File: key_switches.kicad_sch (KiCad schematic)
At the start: 3 parts, among them SW1 SW_Push

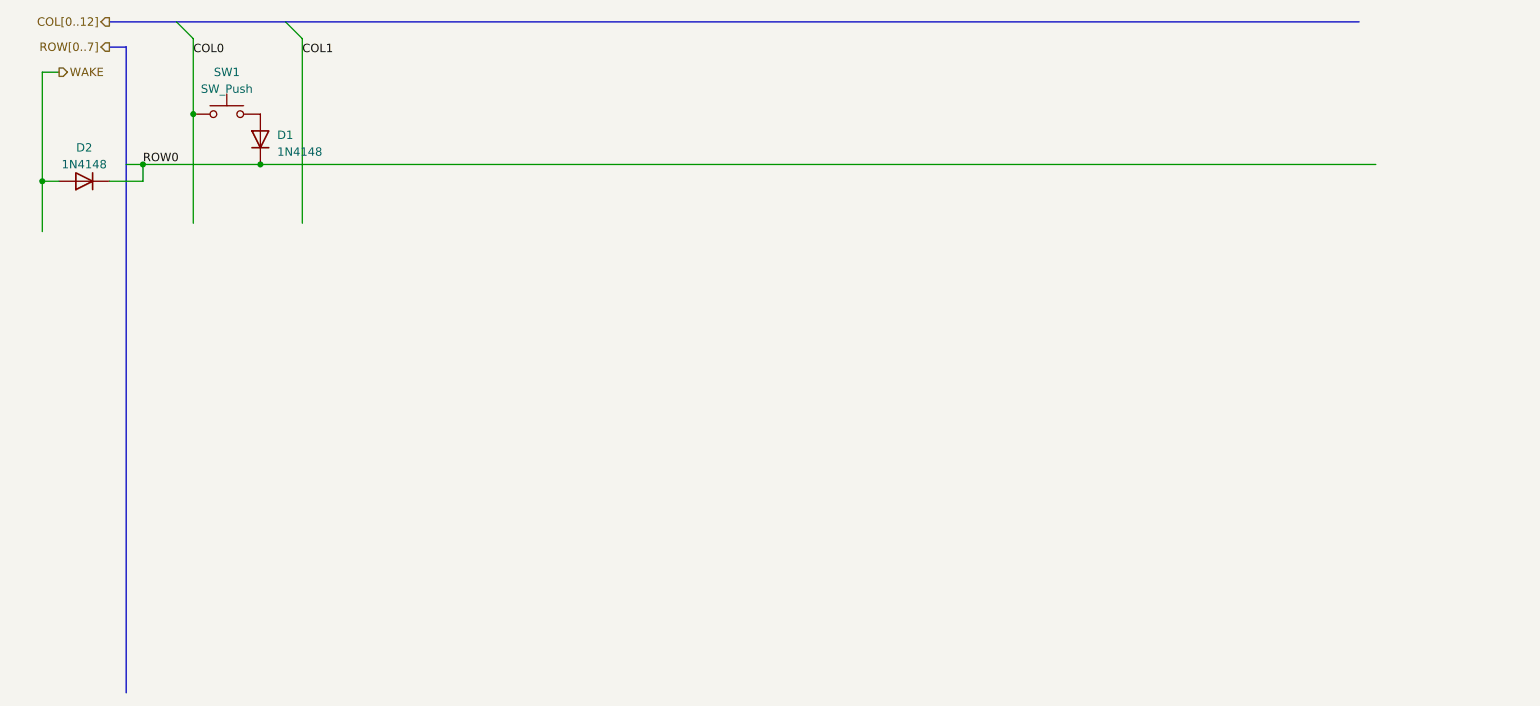
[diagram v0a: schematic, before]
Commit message: added a new key
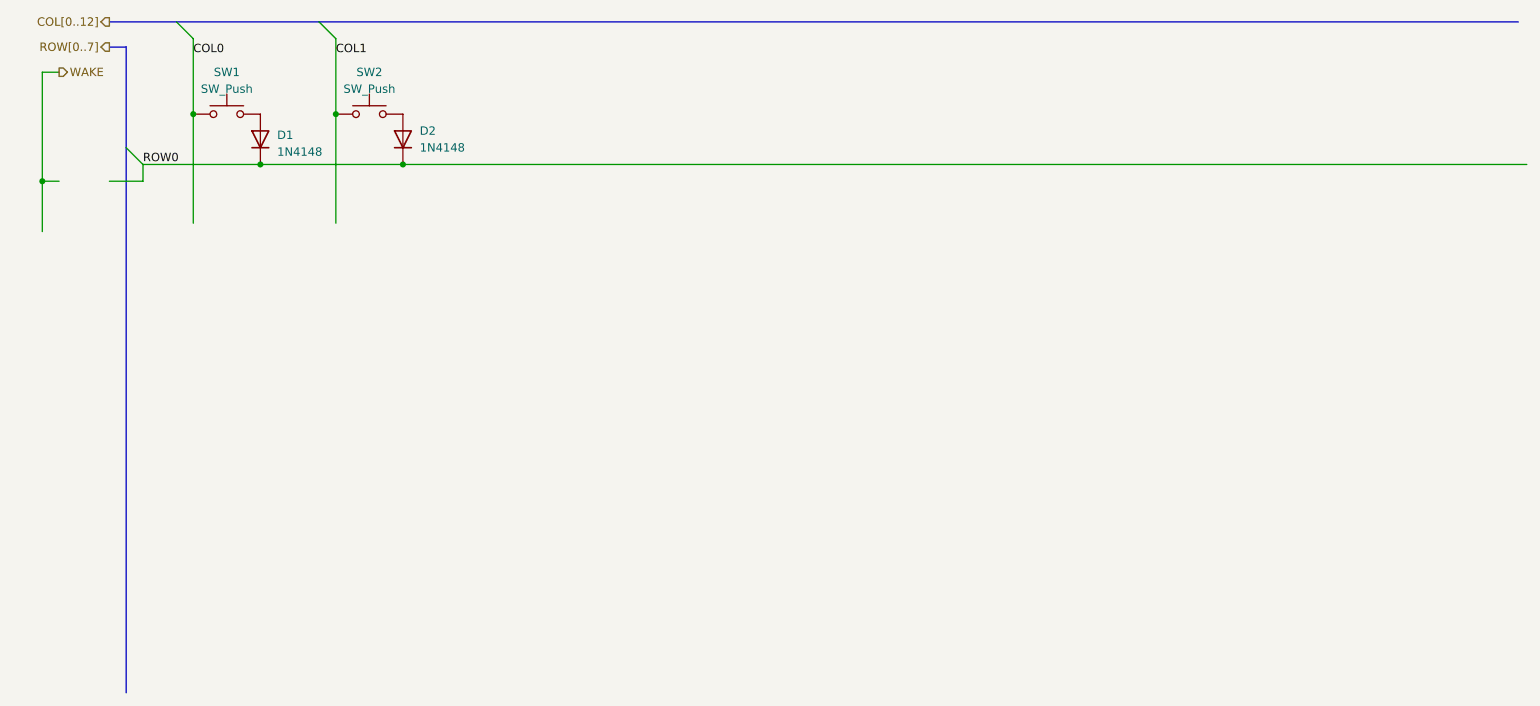
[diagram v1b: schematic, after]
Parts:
- added SW2: SW_Push, symbol Switch:SW_Push
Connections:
- net COL1: now also SW2.1
- net WAKE: no longer D2.2 (A)
- new net: D2.2 (A), SW2.2
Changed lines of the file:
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@@
   (junction (at 19.05 64.77) (diameter 0) (color 0 0 0 0)
   )
+  (junction (at 63.5 54.61) (diameter 0) (color 0 0 0 0)
+  )
   (junction (at 41.91 54.61) (diameter 0) (color 0 0 0 0)
   )
-  (junction (at 34.29 62.23) (diameter 0) (color 0 0 0 0)
+  (junction (at 73.66 62.23) (diameter 0) (color 0 0 0 0)
   )
   (junction (at 52.07 62.23) (diameter 0) (color 0 0 0 0)
@@
     (stroke (width 0) (type default))
   )
-  (bus_entry (at 58.42 43.18) (size -2.54 -2.54)
-    (stroke (width 0) (type default))
-  )
-  (bus (pts (xy 55.88 40.64) (xy 218.44 40.64))
+  (bus_entry (at 63.5 43.18) (size -2.54 -2.54)
+    (stroke (width 0) (type default))
+  )
+  (bus_entry (at 31.75 59.69) (size 2.54 2.54)
+    (stroke (width 0) (type default))
+  )
+  (bus (pts (xy 60.96 40.64) (xy 242.57 40.64))
     (stroke (width 0) (type default))
   )
@@
     (stroke (width 0) (type default))
   )
+  (wire (pts (xy 63.5 43.18) (xy 63.5 54.61))
+    (stroke (width 0) (type default))
+  )
+  (wire (pts (xy 73.66 62.23) (xy 243.84 62.23))
+    (stroke (width 0) (type default))
+  )
+  (wire (pts (xy 19.05 48.26) (xy 19.05 64.77))
+    (stroke (width 0) (type default))
+  )
+  (wire (pts (xy 21.59 48.26) (xy 19.05 48.26))
+    (stroke (width 0) (type default))
+  )
   (wire (pts (xy 34.29 62.23) (xy 52.07 62.23))
     (stroke (width 0) (type default))
   )
-  (wire (pts (xy 58.42 43.18) (xy 58.42 71.12))
-    (stroke (width 0) (type default))
-  )
-  (wire (pts (xy 19.05 48.26) (xy 19.05 64.77))
-    (stroke (width 0) (type default))
-  )
-  (wire (pts (xy 31.75 62.23) (xy 34.29 62.23))
-    (stroke (width 0) (type default))
-  )
-  (wire (pts (xy 21.59 48.26) (xy 19.05 48.26))
-    (stroke (width 0) (type default))
-  )
-  (bus (pts (xy 31.75 44.45) (xy 31.75 142.24))
-    (stroke (width 0) (type default))
-  )
-  (bus (pts (xy 39.37 40.64) (xy 55.88 40.64))
+  (bus (pts (xy 31.75 44.45) (xy 31.75 59.69))
+    (stroke (width 0) (type default))
+  )
+  (bus (pts (xy 39.37 40.64) (xy 60.96 40.64))
     (stroke (width 0) (type default))
   )
@@
     (stroke (width 0) (type default))
   )
-  (wire (pts (xy 52.07 62.23) (xy 220.98 62.23))
+  (wire (pts (xy 52.07 62.23) (xy 73.66 62.23))
+    (stroke (width 0) (type default))
+  )
+  (bus (pts (xy 31.75 59.69) (xy 31.75 142.24))
     (stroke (width 0) (type default))
   )
@@
   )
   (wire (pts (xy 34.29 64.77) (xy 34.29 62.23))
+    (stroke (width 0) (type default))
+  )
+  (wire (pts (xy 63.5 54.61) (xy 63.5 71.12))
     (stroke (width 0) (type default))
   )
@@
     (effects (font (size 1.27 1.27)) (justify left bottom))
   )
-  (label "COL1" (at 58.42 45.72 0) (fields_autoplaced)
+  (label "COL1" (at 63.5 45.72 0) (fields_autoplaced)
     (effects (font (size 1.27 1.27)) (justify left bottom))
   )
@@
     )
   )
-  (symbol (lib_id "Diode:1N4148") (at 25.4 64.77 180) (unit 1)
-    (in_bom yes) (on_board yes) (dnp no) (fields_autoplaced)
-    (property "Reference" "D2" (at 25.4 59.69 0)
-      (effects (font (size 1.27 1.27)))
-    )
-    (property "Value" "1N4148" (at 25.4 62.23 0)
-      (effects (font (size 1.27 1.27)))
-    )
-    (property "Footprint" "Diode_THT:D_DO-35_SOD27_P7.62mm_Horizontal" (at 25.4 64.77 0)
-      (effects (font (size 1.27 1.27)) hide)
-    )
-    (property "Datasheet" "https://assets.nexperia.com/documents/data-sheet/1N4148_1N4448.pdf" (at 25.4 64.77 0)
-      (effects (font (size 1.27 1.27)) hide)
-    )
-    (property "Sim.Device" "D" (at 25.4 64.77 0)
-      (effects (font (size 1.27 1.27)) hide)
-    )
-    (property "Sim.Pins" "1=K 2=A" (at 25.4 64.77 0)
+  (symbol (lib_id "Diode:1N4148") (at 73.66 58.42 90) (unit 1)
+    (in_bom yes) (on_board yes) (dnp no) (fields_autoplaced)
+    (property "Reference" "D2" (at 76.2 57.15 90)
+      (effects (font (size 1.27 1.27)) (justify right))
+    )
+    (property "Value" "1N4148" (at 76.2 59.69 90)
+      (effects (font (size 1.27 1.27)) (justify right))
+    )
+    (property "Footprint" "Diode_THT:D_DO-35_SOD27_P7.62mm_Horizontal" (at 73.66 58.42 0)
+      (effects (font (size 1.27 1.27)) hide)
+    )
+    (property "Datasheet" "https://assets.nexperia.com/documents/data-sheet/1N4148_1N4448.pdf" (at 73.66 58.42 0)
+      (effects (font (size 1.27 1.27)) hide)
+    )
+    (property "Sim.Device" "D" (at 73.66 58.42 0)
+      (effects (font (size 1.27 1.27)) hide)
+    )
+    (property "Sim.Pins" "1=K 2=A" (at 73.66 58.42 0)
       (effects (font (size 1.27 1.27)) hide)
     )
@@
         )
       )
+    )
+  )
+  (symbol (lib_id "Switch:SW_Push") (at 68.58 54.61 0) (unit 1)
+    (in_bom yes) (on_board yes) (dnp no) (fields_autoplaced)
+    (property "Reference" "SW2" (at 68.58 48.26 0)
+      (effects (font (size 1.27 1.27)))
+    )
+    (property "Value" "SW_Push" (at 68.58 50.8 0)
+      (effects (font (size 1.27 1.27)))
+    )
+    (property "Footprint" "" (at 68.58 49.53 0)
+      (effects (font (size 1.27 1.27)) hide)
+    )
+    (property "Datasheet" "~" (at 68.58 49.53 0)
+      (effects (font (size 1.27 1.27)) hide)
+    )
+    (pin "1")
+    (pin "2")
+    (instances
+      (project "Das Keymatrix"
+        (path "/acc36760-ecf2-4bfb-a74b-64a2ca3ad899/b926c080-6ca9-40c9-8789-c9c9b79d063c"
+          (reference "SW2") (unit 1)
+        )
+      )

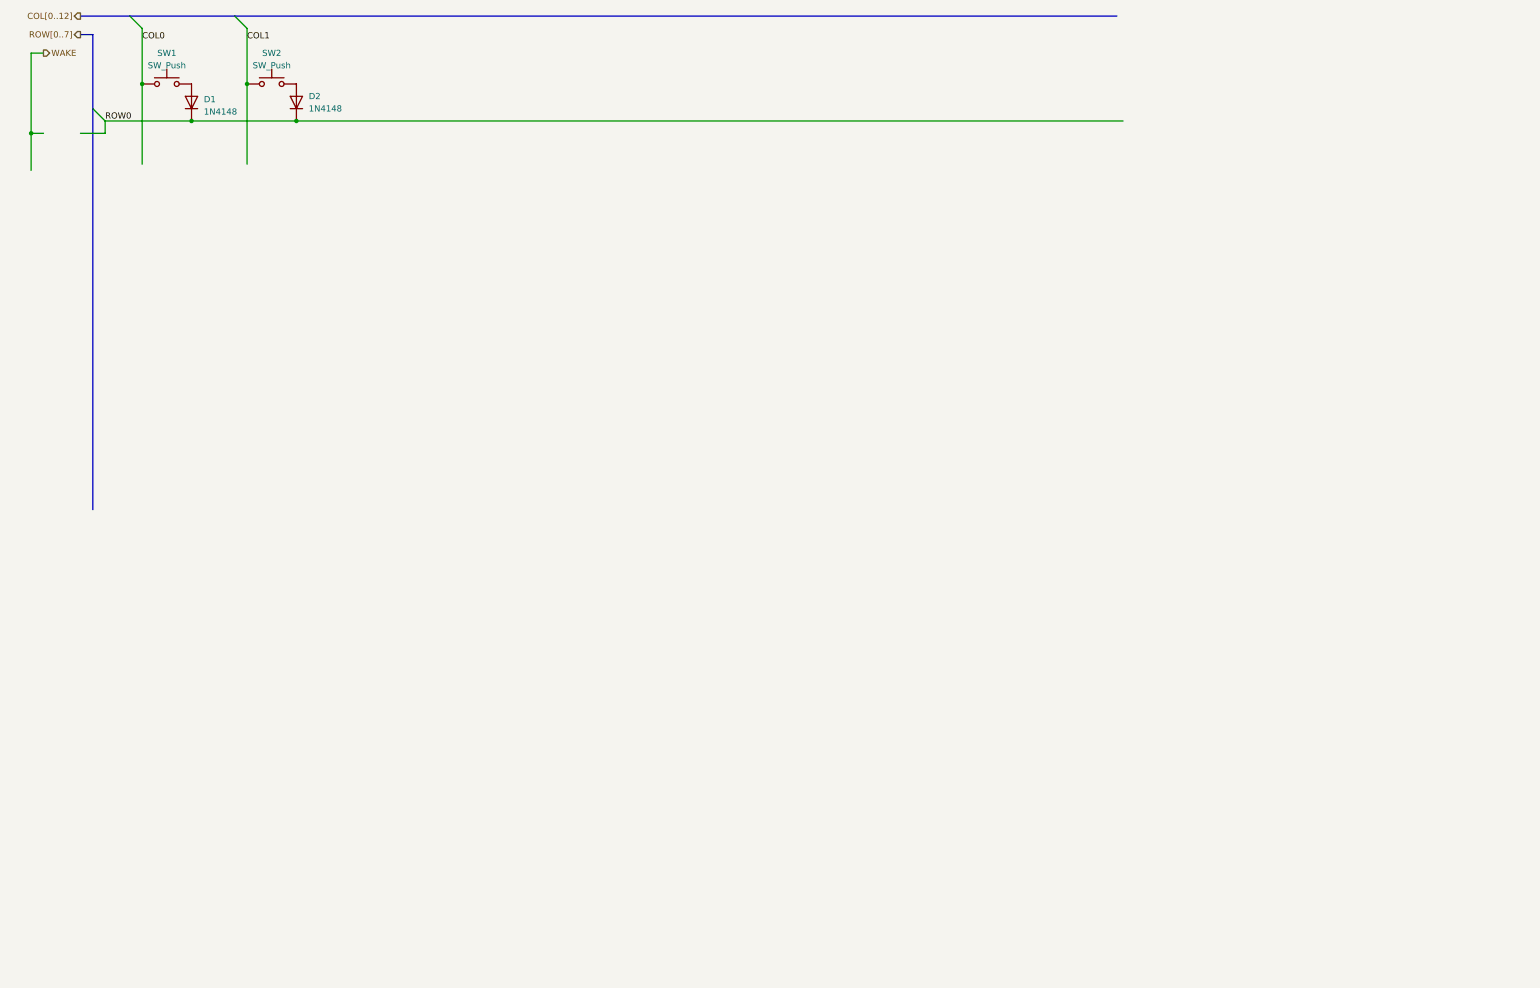
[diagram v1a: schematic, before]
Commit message: added extra switches
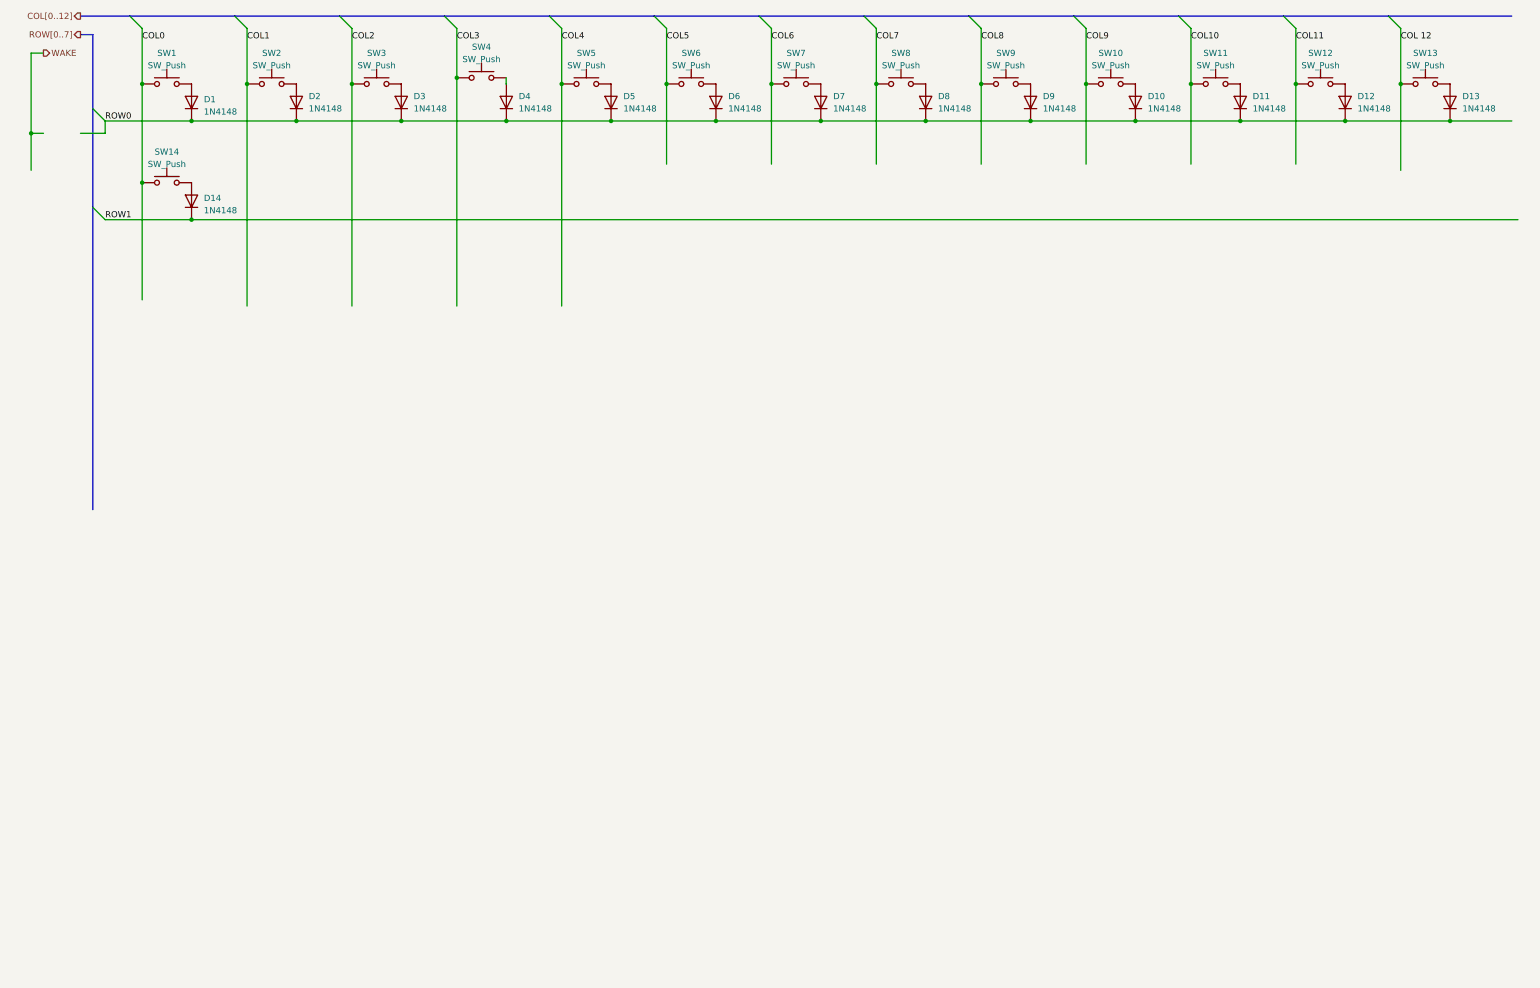
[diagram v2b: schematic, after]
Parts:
- added D10, D11, D12, D13, D14, D3, D4, D5, D6, D7, D8, D9: 1N4148, Diode_THT:D_DO-35_SOD27_P7.62mm_Horizontal, symbol Diode:1N4148
- added SW10, SW11, SW12, SW13, SW14, SW3, SW4, SW5, SW6, SW7, SW8, SW9: SW_Push, symbol Switch:SW_Push
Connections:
- net COL0: now also SW14.1
- net ROW0: now also D10.1 (K), D11.1 (K), D12.1 (K), D13.1 (K), D3.1 (K), D4.1 (K), D5.1 (K), D6.1 (K), D7.1 (K), D8.1 (K), D9.1 (K)
- new net: D9.2 (A), SW9.2
- new net: D7.2 (A), SW7.2
- new net: D12.2 (A), SW12.2
- new net: D5.2 (A), SW5.2
- new net: D6.2 (A), SW6.2
- new net: D14.2 (A), SW14.2
- new net: D10.2 (A), SW10.2
- new net: D13.2 (A), SW13.2
- new net: D4.2 (A), SW4.2
- new net: D8.2 (A), SW8.2
- new net: D3.2 (A), SW3.2
- new net: D11.2 (A), SW11.2
- new net COL 12: SW13.1
- new net COL10: SW11.1
- new net COL11: SW12.1
- new net COL2: SW3.1
- new net COL3: SW4.1
- new net COL4: SW5.1
- new net COL5: SW6.1
- new net COL6: SW7.1
- new net COL7: SW8.1
- new net COL8: SW9.1
- new net COL9: SW10.1
- new net ROW1: D14.1 (K)

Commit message: more changes to keys
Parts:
- added D15, D16, D17, D18, D19, D20, D21, D22, D23, D24, D25, D26: 1N4148, Diode_THT:D_DO-35_SOD27_P7.62mm_Horizontal, symbol Diode:1N4148
- added SW15, SW16, SW17, SW18, SW19, SW20, SW21, SW22, SW23, SW24, SW25, SW26: SW_Push, symbol Switch:SW_Push
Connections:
- net COL 12: now also SW26.1
- net COL1: now also SW15.1
- net COL10: now also SW24.1
- net COL11: now also SW25.1
- net COL2: now also SW16.1
- net COL3: now also SW17.1
- net COL4: now also SW18.1
- net COL5: now also SW19.1
- net COL6: now also SW20.1
- net COL7: now also SW21.1
- net COL8: now also SW22.1
- net COL9: now also SW23.1
- net ROW1: now also D15.1 (K), D16.1 (K), D17.1 (K), D18.1 (K), D19.1 (K), D20.1 (K), D21.1 (K), D22.1 (K), D23.1 (K), D24.1 (K), D25.1 (K), D26.1 (K)
- new net: D20.2 (A), SW20.2
- new net: D17.2 (A), SW17.2
- new net: D15.2 (A), SW15.2
- new net: D23.2 (A), SW23.2
- new net: D21.2 (A), SW21.2
- new net: D19.2 (A), SW19.2
- new net: D18.2 (A), SW18.2
- new net: D24.2 (A), SW24.2
- new net: D22.2 (A), SW22.2
- new net: D25.2 (A), SW25.2
- new net: D16.2 (A), SW16.2
- new net: D26.2 (A), SW26.2
